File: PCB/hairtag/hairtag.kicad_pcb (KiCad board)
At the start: 2 copper layers, 24 x 24 mm, 17 parts, among them J1 Flash, J2 BAT, U1 ESP32-C3FH4, X1 XL2EL89CPI-111YLC-40M

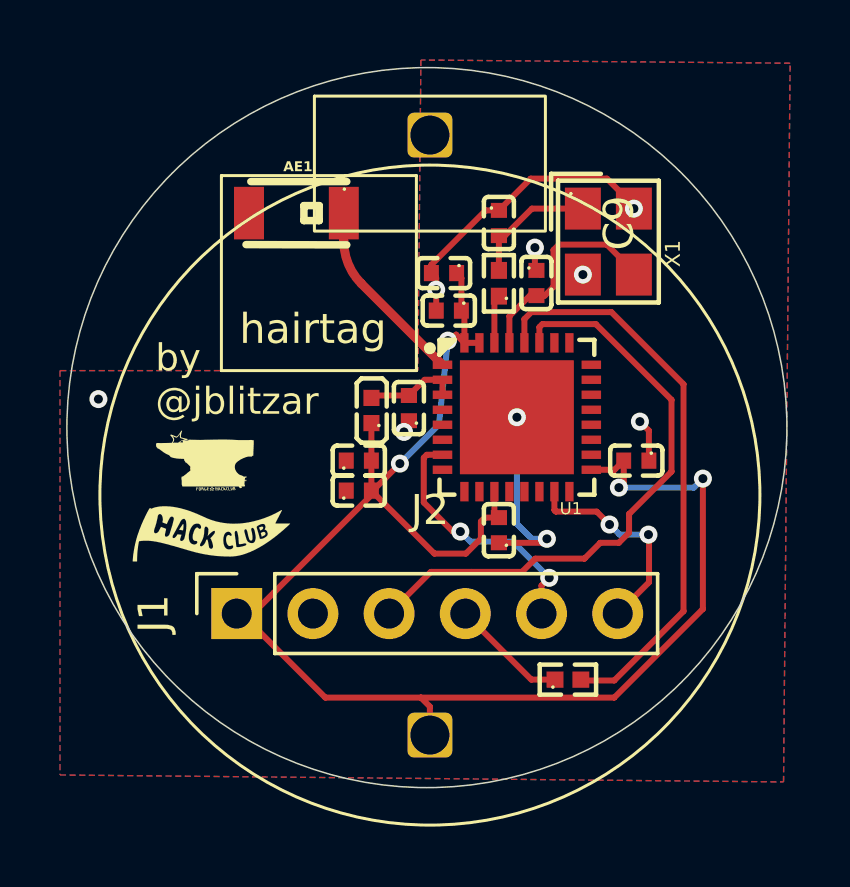
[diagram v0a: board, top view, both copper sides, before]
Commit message: clean up tracks and vias
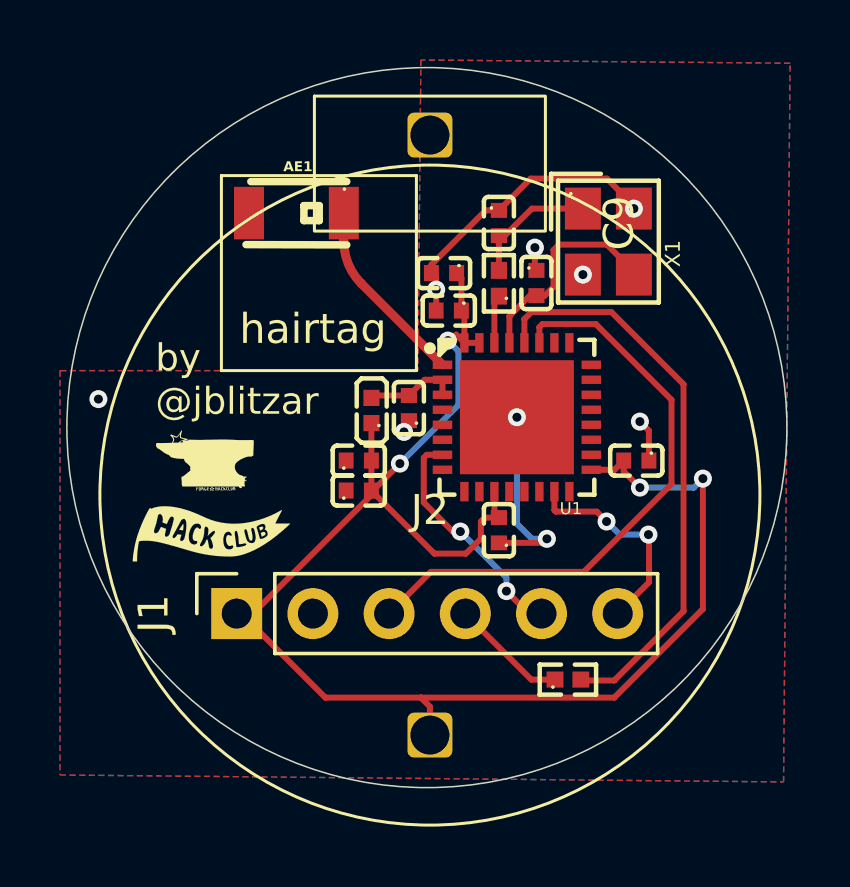
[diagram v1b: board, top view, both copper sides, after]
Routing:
- net /CHIP_EN: track 8.93 -> 7.46 mm
- net /VCC: track 53.6 -> 52.5 mm
- net GND: track 19.9 -> 19.1 mm

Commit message: stuff
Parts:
- J2: moved to B.Cu
- turned J2 to 180 degrees
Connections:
- net /CTS renamed /DTR
- J2 pad 1: /VCC -> GND
- J2 pad 2: GND -> /VCC
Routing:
- net /VCC: track 52.5 -> 70.0 mm
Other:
- board text added: "DTR"
- board text added: "GND"
- board text added: "RTS"
- board text added: "RXD"
- board text added: "TXD"
- board text added: "VCC"

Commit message: blend
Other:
- board text added: "Forged in Valinor"
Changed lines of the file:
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@@
 		(layer "Edge.Cuts")
+	)
+	(gr_text "Forged in Valinor"
+		(at 50.5 59.8 0)
+		(layer "F.SilkS")
+		(effects
+			(font
+				(size 0.4 0.4)
+				(thickness 0.1)
+				(italic yes)
+			)
+			(justify left bottom)
+		)
 	)
 	(gr_text "VCC"

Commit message: Update hairtag.kicad_pcb
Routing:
- net GND: track 19.1 -> 24.8 mm
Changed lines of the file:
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@@
+	)
+	(segment
+		(start 55.2 65.5)
+		(end 55.2 65.65)
+		(width 0.2)
+		(layer "B.Cu")
+		(net "GND")
 	)
 	(segment
@@
 	)
 	(segment
+		(start 51.3 61.6)
+		(end 55.2 65.5)
+		(width 0.2)
+		(layer "B.Cu")
+		(net "GND")
+	)
+	(segment
 		(start 58.1 55.055)
 		(end 58.1 58.608997)
@@
 	)
 	(segment
-		(start 54.9 64.4)
+		(start 51.715044 64.4)
 		(end 61.34441 64.4)
 		(width 0.2)
@@
 		(start 56.35 52.575)
 		(end 56.85 52.575)
-		(width 0.2)
-		(layer "F.Cu")
-		(net "/VCC")
-	)
-	(segment
-		(start 51.715044 64.4)
-		(end 54.9 64.4)
 		(width 0.2)
 		(layer "F.Cu")
@@
 	)
 	(segment
-		(start 60.3 48.1)
-		(end 58.6 48.1)
-		(width 0.2)
-		(layer "F.Cu")
-		(net "Net-(C9-Pad2)")
-	)
-	(segment
-		(start 57.5 49)
-		(end 57.5 50.16)
-		(width 0.2)
-		(layer "F.Cu")
-		(net "Net-(C9-Pad2)")
-	)
-	(segment
-		(start 57.7 49)
-		(end 57.5 49)
-		(width 0.2)
-		(layer "F.Cu")
-		(net "Net-(C9-Pad2)")
-	)
-	(segment
-		(start 58.6 48.1)
-		(end 57.7 49)
-		(width 0.2)
-		(layer "F.Cu")
-		(net "Net-(C9-Pad2)")
-	)
-	(segment
-		(start 55.62 53.305)
-		(end 52.915786 50.600786)
-		(width 0.3)
-		(layer "F.Cu")
-		(net "/LNA_IN")
-	)
-	(segment
-		(start 52.33 49.186573)
-		(end 52.33 48.25)
-		(width 0.3)
-		(layer "F.Cu")
-		(net "/LNA_IN")
-	)
-	(arc
-		(start 52.33 49.186573)
-		(mid 52.482241 49.95194)
-		(end 52.915786 50.600786)
-		(width 0.3)
-		(layer "F.Cu")
-		(net "/LNA_IN")
-	)
-	(segment
-		(start 57.35 51.17)
-		(end 57.35 52.575)
-		(width 0.2)
-		(layer "F.Cu")
-		(net "/XTAL_P")
-	)
-	(segment
 		(start 59.35 57.535)
 		(end 59.35 58.15)
@@
 		(net "/DTR")
 	)
+	(segment
+		(start 60.3 48.1)
+		(end 58.6 48.1)
+		(width 0.2)
+		(layer "F.Cu")
+		(net "Net-(C9-Pad2)")
+	)
+	(segment
+		(start 57.5 49)
+		(end 57.5 50.16)
+		(width 0.2)
+		(layer "F.Cu")
+		(net "Net-(C9-Pad2)")
+	)
+	(segment
+		(start 57.7 49)
+		(end 57.5 49)
+		(width 0.2)
+		(layer "F.Cu")
+		(net "Net-(C9-Pad2)")
+	)
+	(segment
+		(start 58.6 48.1)
+		(end 57.7 49)
+		(width 0.2)
+		(layer "F.Cu")
+		(net "Net-(C9-Pad2)")
+	)
+	(segment
+		(start 55.62 53.305)
+		(end 53.501573 51.186573)
+		(width 0.3)
+		(layer "F.Cu")
+		(net "/LNA_IN")
+	)
+	(arc
+		(start 53.501573 51.186573)
+		(mid 52.634482 49.88888)
+		(end 52.33 48.358146)
+		(width 0.3)
+		(layer "F.Cu")
+		(net "/LNA_IN")
+	)
+	(segment
+		(start 57.35 51.17)
+		(end 57.35 52.575)
+		(width 0.2)
+		(layer "F.Cu")
+		(net "/XTAL_P")
+	)
 	(zone
